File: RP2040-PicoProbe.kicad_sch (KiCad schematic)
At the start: 47 parts, among them J1 CONN_MCU_DEBUG, J2 CONN_DBG_COMB, J5 USB_B_Micro, J7 CONN_DBG_JTAG, U1 W25Q128JVS, U2 RP2040, U3 74AUP1T17, U4 W25Q128JVEIQ, U5 MIC5205-3.3YM5, U6 74AUP1T17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

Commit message: Renamed schematic and board title
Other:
- company: (c) 2023 Andriy Golovnya -> (c) 2024 Andriy Golovnya
- title: RP2040-MicroProbe-0010 -> RP2040-PicoProbe-0010

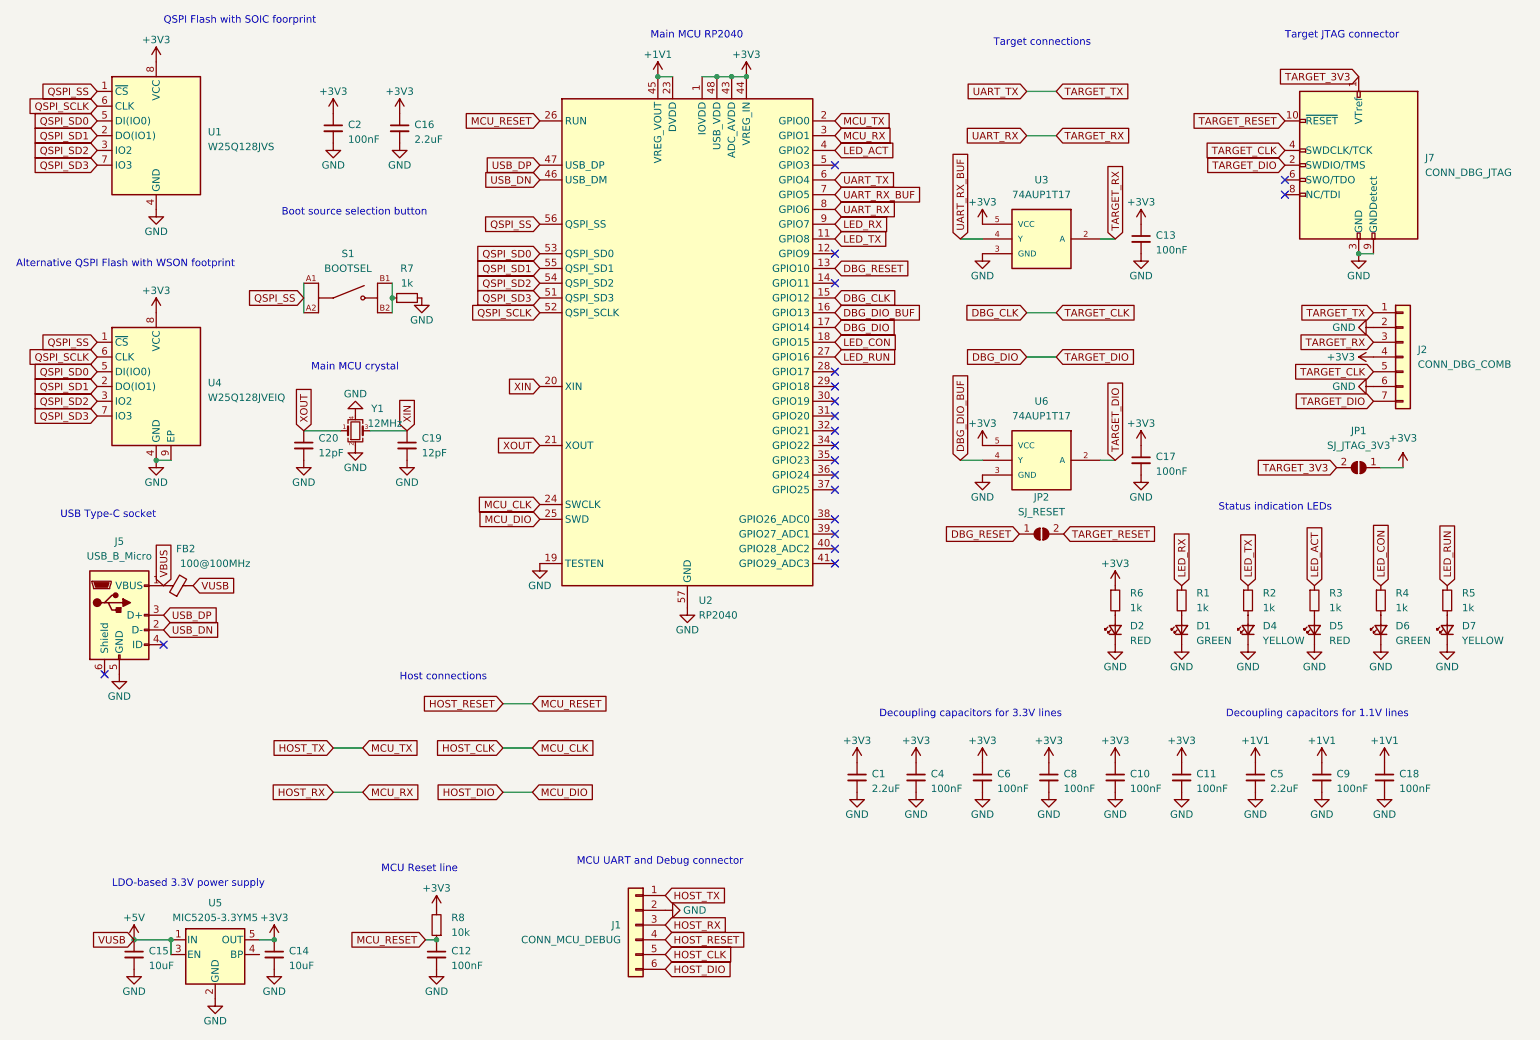
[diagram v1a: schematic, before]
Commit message: Removed host debug part. Moved secondary components to the back of the board.
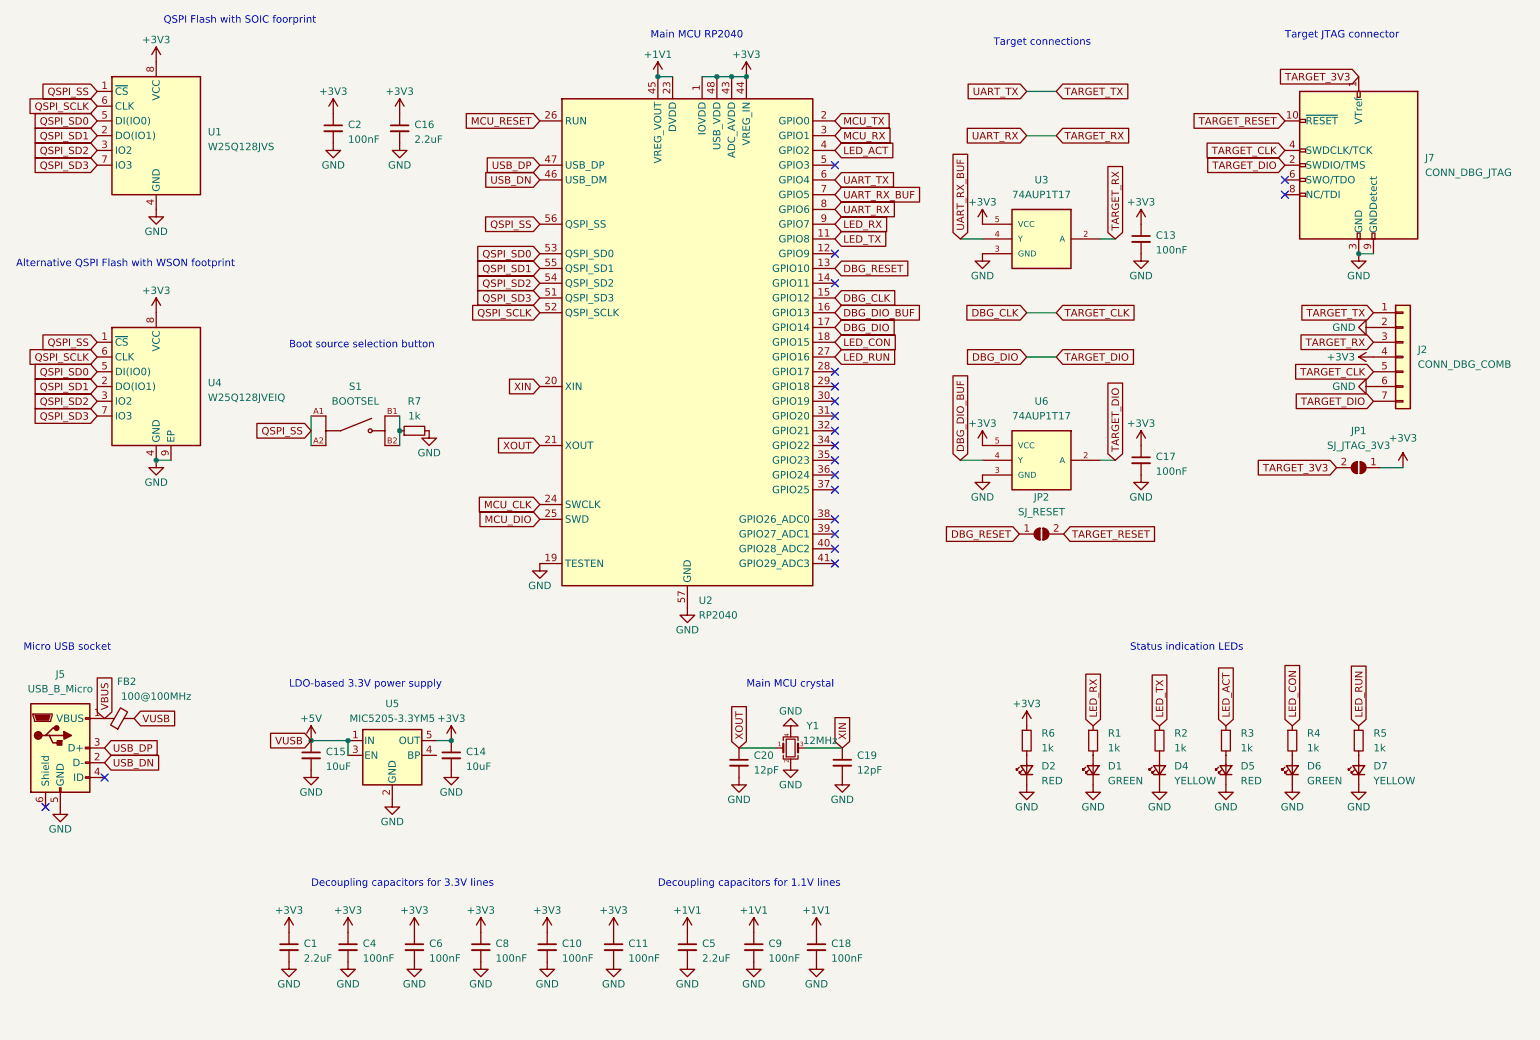
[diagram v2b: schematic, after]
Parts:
- removed C12: 100nF, Capacitor_SMD:C_0402_1005Metric, symbol Device:C_Small
- removed J1: CONN_MCU_DEBUG, Connector_PinHeader_2.54mm:PinHeader_1x06_P2.54mm_Vertical, symbol Connector_Generic:Conn_01x06
- removed R8: 10k, Resistor_SMD:R_0402_1005Metric, symbol Device:R_Small
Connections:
- net HOST_CLK renamed MCU_CLK
- net HOST_DIO renamed MCU_DIO
- net HOST_RESET renamed MCU_RESET
- net HOST_RX renamed MCU_RX
- net HOST_TX renamed MCU_TX
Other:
- note added: "Micro USB socket"
- note removed: "Host connections"
- note removed: "MCU Reset line"
- note removed: "MCU UART and Debug connector"
- note removed: "USB Type-C socket"
- moved on the sheet: C1, C10, C11, C14, C15, C18, C19, C20, C4, C5, C6, C8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

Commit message: Roughly put components to their places
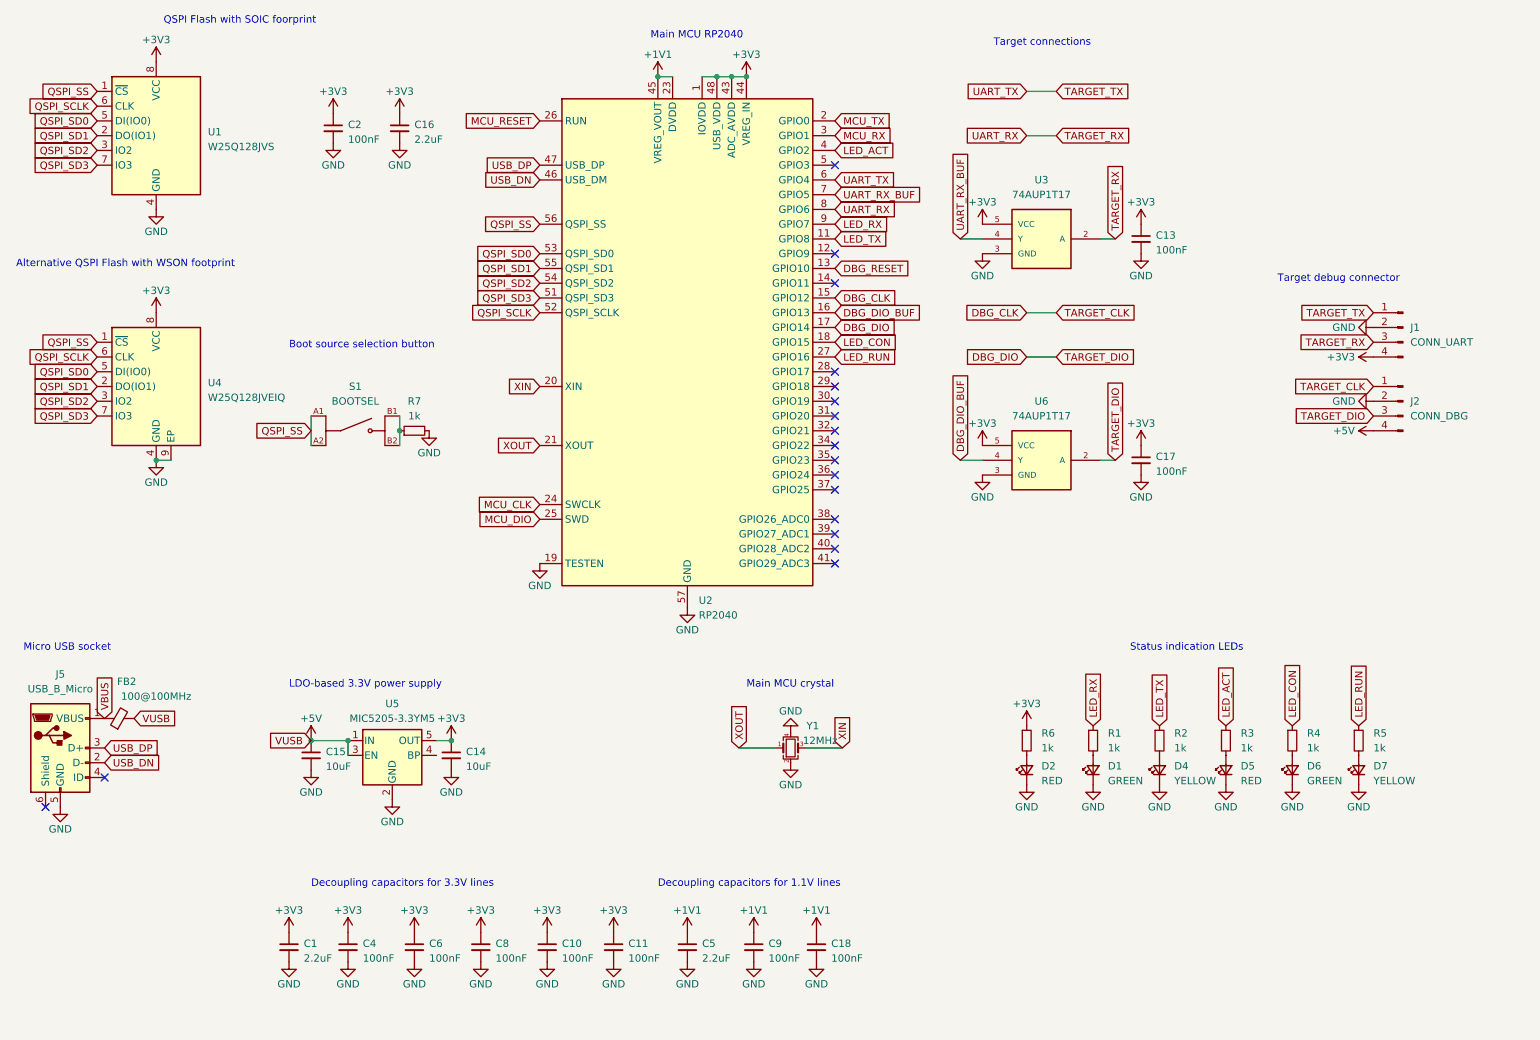
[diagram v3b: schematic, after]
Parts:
- removed C19, C20: 12pF, Capacitor_SMD:C_0402_1005Metric, symbol Device:C_Small
- removed J2: CONN_DBG_COMB, Connector_PinSocket_2.54mm:PinSocket_1x07_P2.54mm_Vertical, symbol Connector_Generic:Conn_01x07
- removed J7: CONN_DBG_JTAG, Connector_PinHeader_1.27mm:PinHeader_2x05_P1.27mm_Vertical_SMD, symbol Connector:Conn_ARM_JTAG_SWD_10
- removed JP1: SJ_JTAG_3V3, Jumper:SolderJumper-2_P1.3mm_Open_TrianglePad1.0x1.5mm, symbol Jumper:SolderJumper_2_Open
- removed JP2: SJ_RESET, Jumper:SolderJumper-2_P1.3mm_Open_TrianglePad1.0x1.5mm, symbol Jumper:SolderJumper_2_Open
- added J1: CONN_UART, Connector_Harwin:Harwin_M20-89004xx_1x04_P2.54mm_Horizontal, symbol Connector:Conn_01x04_Pin
- added J2: CONN_DBG, Connector_Harwin:Harwin_M20-89004xx_1x04_P2.54mm_Horizontal, symbol Connector:Conn_01x04_Pin
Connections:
- net +3V3: now also J1.4 (Pin_4)
- net +5V: now also J2.4 (Pin_4)
- net DBG_CLK: now also J2.1 (Pin_1)
- net DBG_DIO: now also J2.3 (Pin_3)
- net GND: now also J1.2 (Pin_2), J2.2 (Pin_2)
- net TARGET_RX: now also J1.3 (Pin_3)
- net TARGET_TX: now also J1.1 (Pin_1)
- no-connect marks 20 -> 18
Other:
- note added: "Target debug connector"
- note removed: "Target JTAG connector"

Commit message: Moved stuff around
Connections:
- net MCU_CLK: no longer names the net of U2.24 (SWCLK)
- net MCU_DIO: no longer names the net of U2.25 (SWD)
- net MCU_RX: no longer names the net of U2.3 (GPIO1)
- net MCU_TX: no longer names the net of U2.2 (GPIO0)
- no-connect marks 18 -> 22
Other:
- moved on the sheet: C1, C10, C11, C13, C14, C15, C17, C18, C4, C5, C6, C8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
